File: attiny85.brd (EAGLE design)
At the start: 74.7 x 55.5 mm, 8 parts, among them U1 TINY85-20-DIP

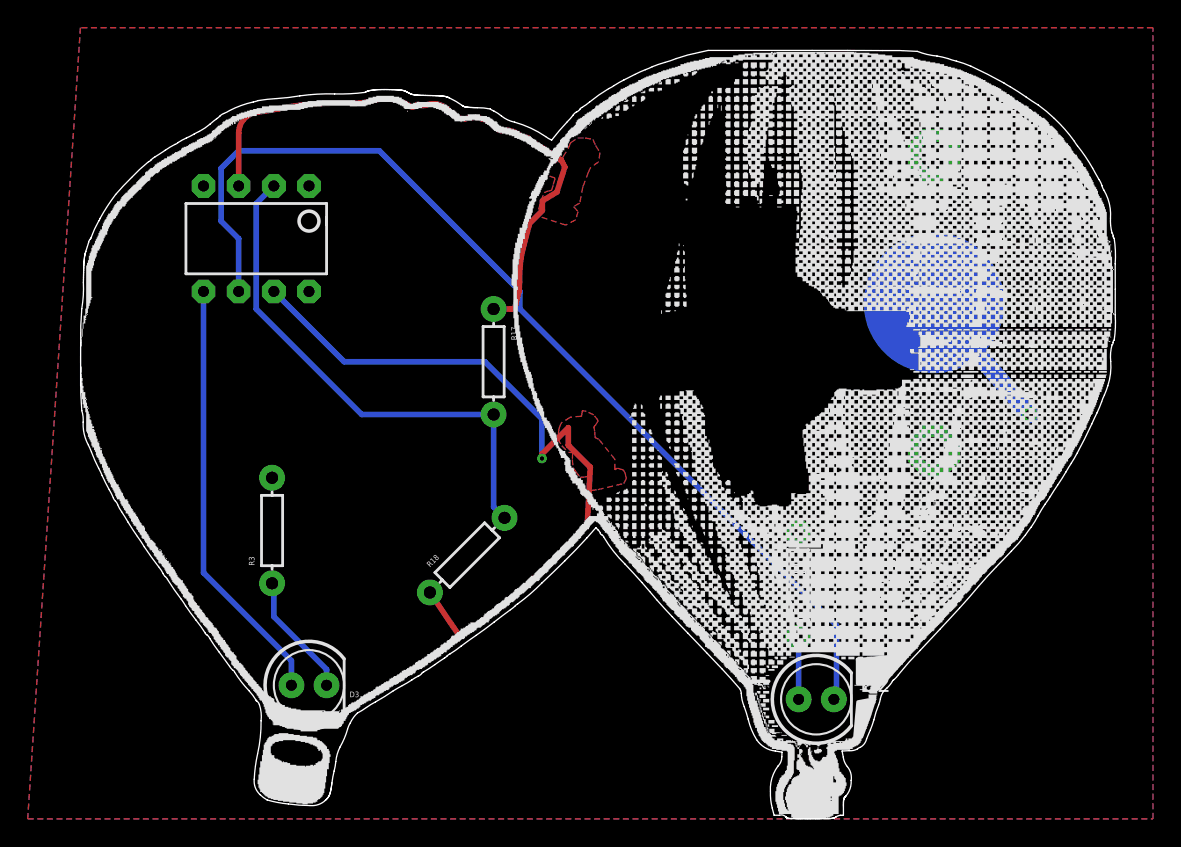
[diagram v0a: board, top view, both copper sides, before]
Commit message: Minor Cleanups - Silkscreen & Battery Holder
Battery Holder: Updated so that the rest of the plane isn't also
		exposed on the board

Silkscreen: mostly minor adjustments, and exposing the right led
		resistor
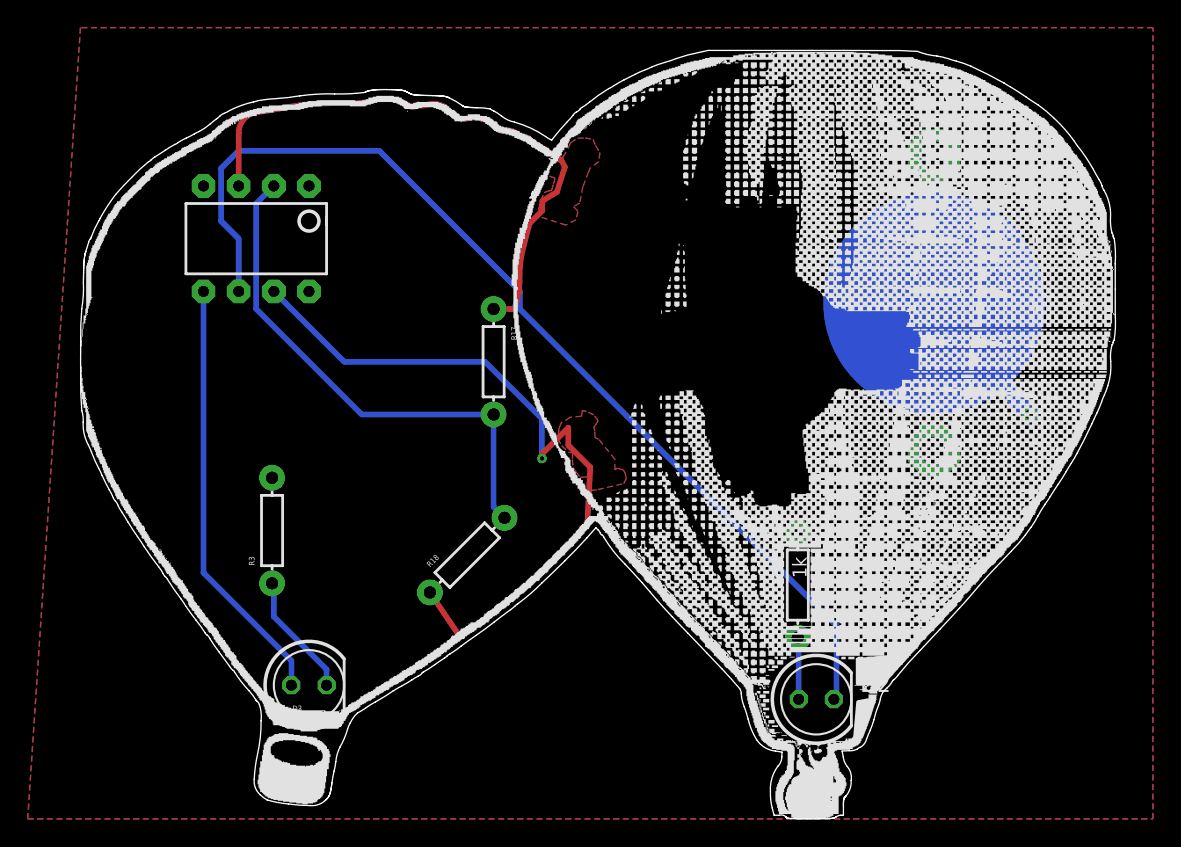
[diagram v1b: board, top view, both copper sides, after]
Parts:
- BAT1: device adafruit:CR2032-THRU -> adafruit-john modded:CR2032-THRU
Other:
- board text added: "+ Long Anode"
- board text added: "- Short Cathode Flat Side"
- board text added: "CR2032"
- board text added: "Designed by John 'Warthog9' Hawley Licensed CC-BY-SA 4.0 in 2016 https://github.com/warthog9/ABQMMF-Solderkit-2016"
- board text removed: "Designed by John 'Warthog9' Hawley Licensed CC-BY-SA 4.0 in 2016"
